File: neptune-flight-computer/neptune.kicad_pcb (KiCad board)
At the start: 4 copper layers, 39 x 60 mm, 65 parts, among them J1 THD2528-11SD-GF, J2 Conn_01x02, J3 Conn_Coaxial, J4 USB_B_Micro, J5 Conn_01x04, J6 Conn_01x04, J7 Conn_01x04, Q1 Si2301-TP, Q2 AO3401A, SW1 TS-1187A-B-A-B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

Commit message: Changes
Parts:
- moved C1 25.9 mm to (130.2, 112.8)
- moved C3 25.9 mm to (131.2, 108.8)
- moved C10 25.9 mm to (128.7, 94.8)
- moved C22 25.9 mm to (130.5, 94.8)
- moved C23 25.9 mm to (132.2, 94.8)
- moved C13 25.9 mm to (122.3, 94.5)
- moved C16 25.9 mm to (122.3, 96.5)
- moved C17 25.9 mm to (100.8, 91.5)
- moved C2 25.9 mm to (123.2, 112.8)
- moved C21 25.9 mm to (122.2, 108.8)
- moved C6 25.9 mm to (119.3, 93.0)
- moved D3 25.9 mm to (102.1, 100.8)
- moved G*** 25.9 mm to (123.5, 86.4)
- moved J4 25.9 mm to (101.6, 110.2)
- moved J6 25.9 mm to (100.5, 122.8)
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
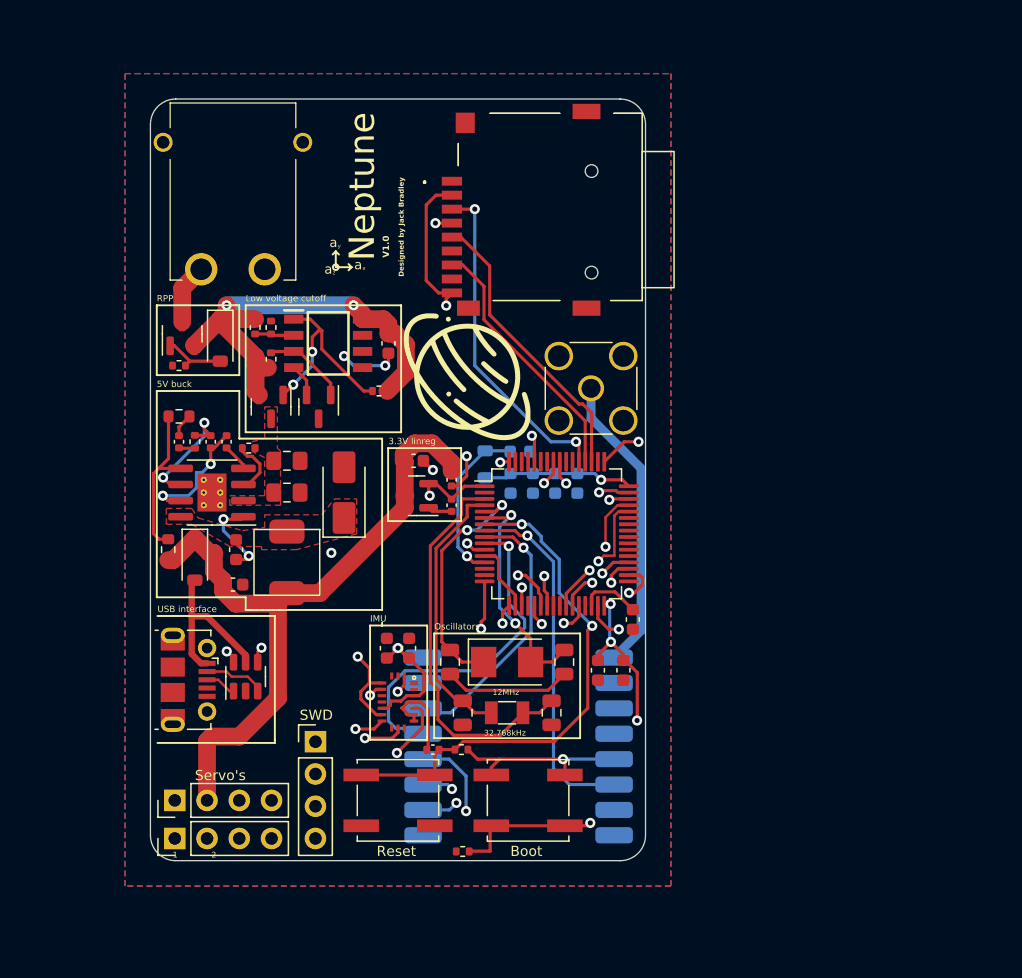
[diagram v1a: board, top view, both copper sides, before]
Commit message: Added mounting holes
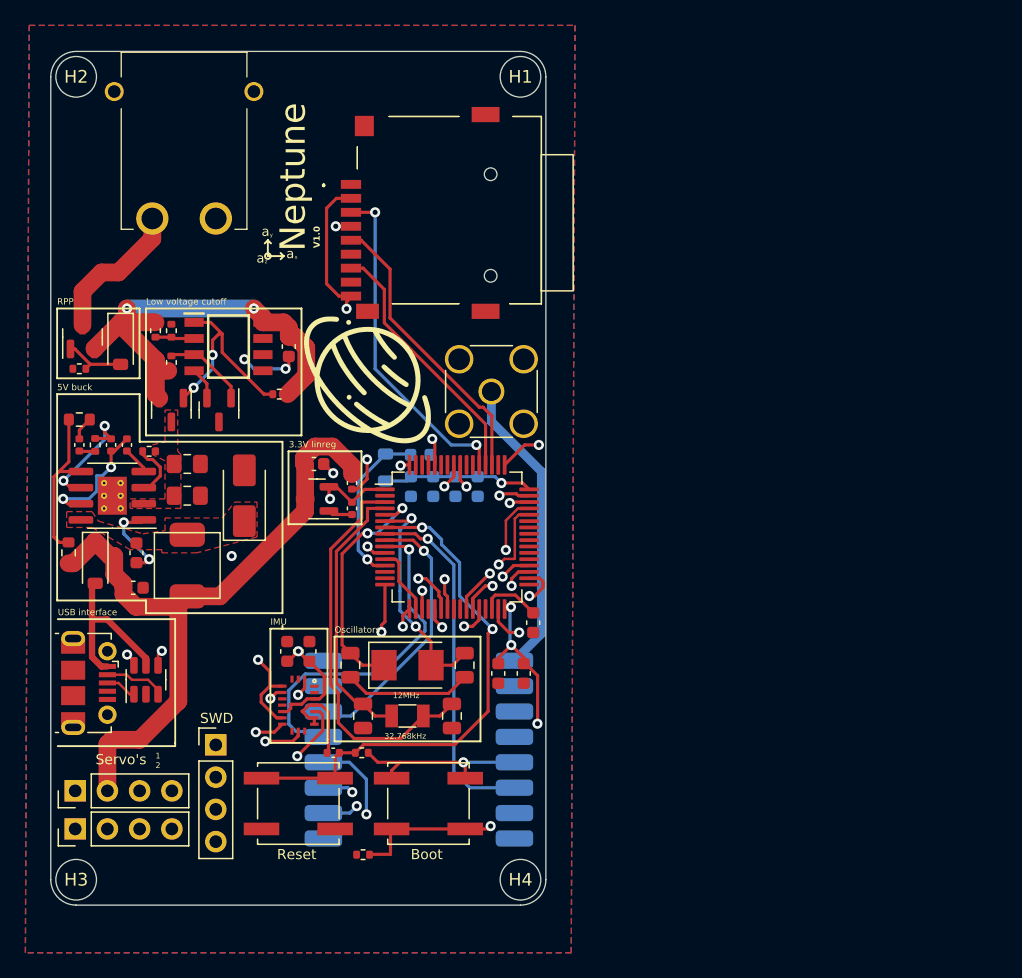
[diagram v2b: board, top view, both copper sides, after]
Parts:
- added H1: MountingHole, MountingHole:MountingHole_3.2mm_M3, F.Cu at (127.8, 62.8)
- added H2: MountingHole, MountingHole:MountingHole_3.2mm_M3, F.Cu at (92.8, 62.8)
- added H3: MountingHole, MountingHole:MountingHole_3.2mm_M3, F.Cu at (92.8, 126.0)
- added H4: MountingHole, MountingHole:MountingHole_3.2mm_M3, F.Cu at (127.8, 126.0)
- moved J1 7.95 mm to (122.2, 73.2)
- moved J6 7.89 mm to (92.7, 122.0)
- moved J7 7.89 mm to (92.7, 119.0)
- moved C4 7.85 mm to (128.0, 109.8)
- moved C13 7.85 mm to (114.5, 94.8)
- moved C16 7.85 mm to (114.5, 96.8)
- moved C2 7.85 mm to (115.3, 113.1)
- moved C21 7.85 mm to (114.3, 109.1)
- moved C6 7.85 mm to (111.5, 93.2)
- moved J3 7.85 mm to (125.5, 87.5)
- moved R10 7.85 mm to (115.3, 124.0)
- moved U3 7.85 mm to (95.6, 95.8)
- moved U4 7.85 mm to (111.7, 96.0)
- moved Y1 7.85 mm to (118.8, 113.1)
- moved Y2 7.85 mm to (118.8, 109.1)
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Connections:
- C10 pad 1: +3.3V -> +3V3
- C22 pad 1: +3.3V -> +3V3
- C23 pad 1: +3.3V -> +3V3
- C24 pad 1: +3.3V -> +3V3
- C25 pad 1: +3.3V -> +3V3
- C9 pad 1: +3.3V -> +3V3
- J5 pad 1: +3.3V -> +3V3
- L2 pad 1: +3.3V -> +3V3
- R11 pad 2: +3.3V -> +3V3
- SW1 pad 2: +3.3V -> +3V3
- U7 pad 1: +3.3V -> +3V3
- U7 pad 19: +3.3V -> +3V3
- U7 pad 32: +3.3V -> +3V3
- U7 pad 48: +3.3V -> +3V3
- U7 pad 64: +3.3V -> +3V3
- U8 pad 13: +3.3V -> +3V3
- U8 pad 3: +3.3V -> +3V3
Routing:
- net +3V3: track 0.00 -> 23.6 mm, vias 0 -> 4
- net +3.3V: track 58.5 -> 34.9 mm, vias 10 -> 6
- net Net-(J2-Pin_1): track 4.77 -> 11.5 mm
- net +5V: track 58.8 -> 57.8 mm
- net /STM32/S2_feedback: track 28.6 -> 27.6 mm
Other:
- board size 39 x 60 mm -> 39 x 67.2 mm

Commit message: Created production files
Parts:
- C16: value 2.2u -> 1u
- U4: value AP2210N-3.3TRG1 -> LP3993-33B3F
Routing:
- net GND: track 53.5 -> 56.0 mm, vias 9 -> 12
- net /CS_SD: track 32.9 -> 34.0 mm
- net +3V3: vias 4 -> 0
- net +3.3V: vias 6 -> 10
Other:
- board text added: "JLCJLCJLC"

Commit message: Headaches
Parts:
- Y2: footprint Crystal:Crystal_SMD_5032-2Pin_5.0x3.2mm -> Crystal:Crystal_SMD_5032-4Pin_5.0x3.2mm
- moved Y2 0.10 mm to (118.8, 109.0)
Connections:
- C10 pad 1: +3V3 -> +3.3V
- C22 pad 1: +3V3 -> +3.3V
- C23 pad 1: +3V3 -> +3.3V
- C24 pad 1: +3V3 -> +3.3V
- C25 pad 1: +3V3 -> +3.3V
- C9 pad 1: +3V3 -> +3.3V
- J5 pad 1: +3V3 -> +3.3V
- L2 pad 1: +3V3 -> +3.3V
- R11 pad 2: +3V3 -> +3.3V
- SW1 pad 2: +3V3 -> +3.3V
- U7 pad 1: +3V3 -> +3.3V
- U7 pad 19: +3V3 -> +3.3V
- U7 pad 32: +3V3 -> +3.3V
- U7 pad 48: +3V3 -> +3.3V
- U7 pad 64: +3V3 -> +3.3V
- U8 pad 13: +3V3 -> +3.3V
- U8 pad 3: +3V3 -> +3.3V
- Y2 pad 2: /STM32/OSC_OUT -> GND
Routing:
- net +3.3V: track 34.9 -> 58.5 mm
- net +3V3: track 23.6 -> 0.00 mm
- net GND: track 56.0 -> 62.1 mm
- net /STM32/OSC_OUT: track 18.2 -> 16.9 mm
- net /STM32/OSC_IN: track 19.0 -> 19.5 mm

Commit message: Final PCB changes
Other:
- board text added: "JLCJLCJLCJLC"
- board text removed: "JLCJLCJLC"
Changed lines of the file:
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@@
     (effects (font (size 0.5 0.5) (thickness 0.125)) (justify left bottom))
   )
-  (gr_text "JLCJLCJLC" (at 121.65 77 90) (layer "F.SilkS")
+  (gr_text "JLCJLCJLCJLC" (at 121.75 78 90) (layer "F.SilkS")
     (effects (font (size 1 1) (thickness 0.15)) (justify left bottom))
   )
